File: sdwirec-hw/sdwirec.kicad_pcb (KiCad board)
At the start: 4 copper layers, 23.4 x 49.4 mm, 61 parts, among them IC1 USB2640-HZH-02, IC2 MC74HC1G04DTT1G, J1 USB_C_Receptacle_USB2.0, J2 usd_plug, J3 Micro_SD_Card, Q1 SMMBT4403L, Q2 SMMBT4403L, U1 M24C02-RDW, U2 SPX3819M5-L-3-3, U3 TS3A27518EPW, U4 FT200XD, Y1 24Mhz

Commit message: Rev 1.2
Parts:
- added C26: 4.7uF, Capacitor_SMD:C_0603_1608Metric, F.Cu at (143.8, 104.1)
- added C27: 4.7uF, Capacitor_SMD:C_0603_1608Metric, F.Cu at (156.5, 109.2)
- added C28: 100nF, Capacitor_SMD:C_0402_1005Metric, F.Cu at (154.7, 96.1)
- added C29: 100nF, Capacitor_SMD:C_0402_1005Metric, F.Cu at (146.3, 122.1)
- added G***: LOGO, sdwirec:badgerd-logo-9mm, F.Cu at (145.5, 85.2)
- added R18: 1M, Resistor_SMD:R_0402_1005Metric, F.Cu at (143.1, 110.0)
- added R19: 0R, Resistor_SMD:R_0402_1005Metric, F.Cu at (157.2, 113.2)
- added REF**: Tab, KiKit:Tab, F.Cu at (159.0, 102.9)
- added REF**: Tab, KiKit:Tab, F.Cu at (132.5, 116.3)
- added REF**: Tab, KiKit:Tab, F.Cu at (132.5, 102.9)
- added REF**: Tab, KiKit:Tab, F.Cu at (159.0, 116.3)
- added REF**: ESD-Logo_6.6x6mm_SilkScreen, Symbol:ESD-Logo_6.6x6mm_SilkScreen, B.Cu at (146.6, 94.7)
- D1: value LED_Small -> Red
- D3: value Green -> Blue
- FB1, FB2: value 180R -> 150R; footprint LED_SMD:LED_0603_1608Metric -> Diode_SMD:D_0603_1608Metric
- moved C15 6.75 mm to (156.1, 104.5), turned to 90 degrees
- moved C12 3.13 mm to (156.1, 107.0)
- moved C3 3.06 mm to (138.2, 110.5), turned to -90 degrees
- moved C19 1.60 mm to (143.7, 106.5), turned to 180 degrees
- moved R5 1.10 mm to (143.7, 107.8), turned to 0 degrees
- moved C6 0.63 mm to (140.6, 113.0)
- moved Y1 0.56 mm to (140.6, 110.3)
- moved C14 0.22 mm to (142.1, 114.7)
- moved C10 0.18 mm to (143.3, 114.7)
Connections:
- IC1 pad 13: unconnected-(IC1-Pad13) -> Net-(IC1-Pad13)
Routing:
- net +3V3: track 144.3 -> 165.0 mm, vias 19 -> 21
- net Net-(IC1-Pad13): track 0.00 -> 5.39 mm
- net /dSD_DAT3: track 20.7 -> 25.7 mm
- net GND: track 78.0 -> 82.8 mm, vias 35 -> 53
- net Net-(C12-Pad1): track 3.51 -> 8.23 mm
- net /dSD_DAT0: track 21.8 -> 25.6 mm
- net /SD_nCD: track 29.3 -> 33.1 mm
- net /dSD_DAT2: track 22.1 -> 25.7 mm
- net Net-(C29-Pad1): track 18.7 -> 20.7 mm
- net /dSD_CLK: track 23.8 -> 25.7 mm
- net /dSD_DAT1: track 24.1 -> 25.7 mm
- net /VDD: track 20.9 -> 22.2 mm
- net /USB_UP-: track 13.5 -> 12.4 mm
- net /nRESET: track 3.48 -> 2.61 mm
- net /XTAL2: track 8.52 -> 9.11 mm
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- added copper zone on B.Cu, net GND
- added copper zone on F.Cu, net GND
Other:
- board size 23.4 x 49.4 mm -> 26 x 49.9 mm
- board text added: "Rev. 1.2"
- board text added: "`"

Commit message: Rev 1.3
Signed-off-by: Talha Can Havadar <talha.can.havadar@canonical.com>
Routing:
- net GND: vias 53 -> 54
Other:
- board text added: "+"
- board text added: "Rev. 1.3"
- board text removed: "Rev. 1.2"

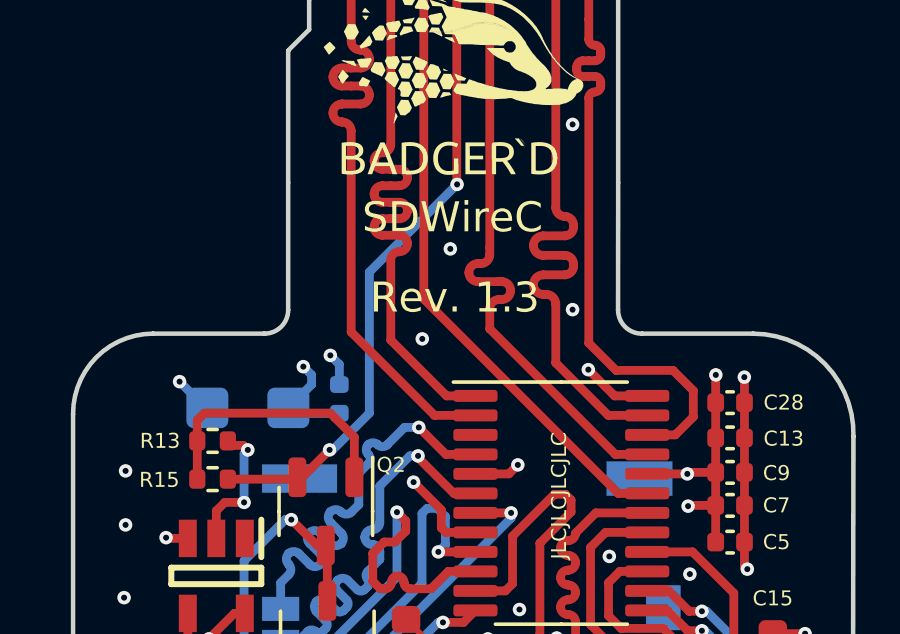
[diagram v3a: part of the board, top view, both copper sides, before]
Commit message: squash! add schottky diode on vdd_device line
Signed-off-by: Talha Can Havadar <havadartalha@gmail.com>
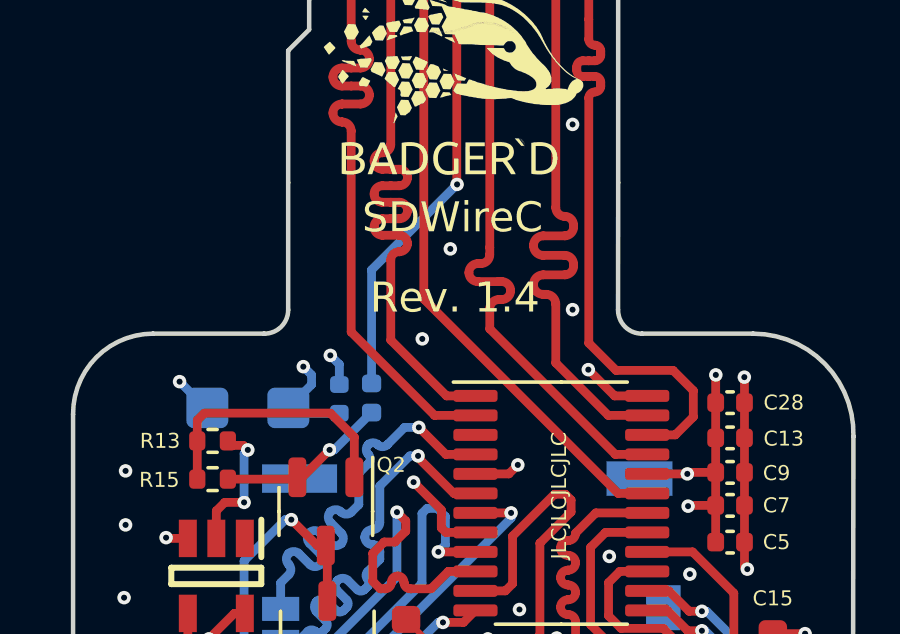
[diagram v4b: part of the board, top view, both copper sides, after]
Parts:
- added D5: D_Schottky_Small_Filled, Diode_SMD:D_0402_1005Metric, B.Cu at (142.7, 95.9)
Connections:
- J2 pad 4: /VDD_DEVICE -> Net-(J2-Pad4)
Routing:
- net /VDD_DEVICE: track 26.6 -> 5.71 mm, vias 2 -> 1
- net Net-(J2-Pad4): track 0.00 -> 19.9 mm, vias 0 -> 1
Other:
- board text added: "Rev. 1.4"
- board text removed: "Rev. 1.3"
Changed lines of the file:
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@@
   (title_block
     (title "Badgerd-SDWireC")
-    (date "2023-07-17")
-    (rev "1.3")
+    (date "2024-09-06")
+    (rev "1.4")
     (company "Badgerd Technologies B.V.")
     (comment 1 "Talha Can Havadar")
@@
   (net 77 "Net-(Q1-Pad1)")
   (net 78 "Net-(IC1-Pad13)")
+  (net 79 "Net-(J2-Pad4)")
   (footprint "KiKit:Tab" (layer "F.Cu")
     (at 159.03 102.9 180)
@@
     (property "Sheetfile" "sdwirec.kicad_sch")
     (property "Sheetname" "")
-    (attr through_hole exclude_from_pos_files)
+    (attr through_hole exclude_from_pos_files exclude_from_bom)
     (fp_text reference "J2" (at 3.79 2.35) (layer "F.SilkS") hide
       (effects (font (size 1 1) (thickness 0.15)))
@@
       (net 58 "/dSD_CMD") (pinfunction "Pin_3") (pintype "passive"))
     (pad "4" smd rect (at 3.3 -0.15) (size 0.8 3.2) (layers "F.Cu" "F.Mask")
-      (net 59 "/VDD_DEVICE") (pinfunction "Pin_4") (pintype "passive"))
+      (net 79 "Net-(J2-Pad4)") (pinfunction "Pin_4") (pintype "passive"))
     (pad "5" smd rect (at 4.4 0) (size 0.8 2.9) (layers "F.Cu" "F.Mask")
       (net 60 "/dSD_CLK") (pinfunction "Pin_5") (pintype "passive"))
@@
     )
   )
+  (footprint "Diode_SMD:D_0402_1005Metric" (layer "B.Cu")
+    (at 142.7 95.92 90)
+    (descr "Diode SMD 0402 (1005 Metric), square (rectangular) end terminal, IPC_7351 nominal, (Body size source: http://www.tortai-tech.com/upload/download/2011102023233369053.pdf), generated with kicad-footprint-generator")
+    (tags "diode")
+    (property "LCSC Part" "C2837790")
+    (property "Sheetfile" "sdwirec.kicad_sch")
+    (property "Sheetname" "")
+    (attr smd)
+    (fp_text reference "D5" (at 0 1.17 90) (layer "B.SilkS")
+      (effects (font (size 0.5 0.5) (thickness 0.1)) (justify mirror))
+    )
+    (fp_text value "D_Schottky_Small_Filled" (at 0 -1.17 90) (layer "B.Fab")
+      (effects (font (size 1 1) (thickness 0.15)) (justify mirror))
+    )
+    (fp_text user "${REFERENCE}" (at 0 0 90) (layer "B.Fab")
+      (effects (font (size 0.25 0.25) (thickness 0.04)) (justify mirror))
+    )
+    (fp_circle (center -1.09 0) (end -1.04 0) (layer "B.SilkS") (width 0.1) (fill none))
+    (fp_line (start -0.93 -0.47) (end -0.93 0.47) (layer "B.CrtYd") (width 0.05))
+    (fp_line (start -0.93 0.47) (end 0.93 0.47) (layer "B.CrtYd") (width 0.05))
+    (fp_line (start 0.93 -0.47) (end -0.93 -0.47) (layer "B.CrtYd") (width 0.05))
+    (fp_line (start 0.93 0.47) (end 0.93 -0.47) (layer "B.CrtYd") (width 0.05))
+    (fp_line (start 0.5 -0.25) (end -0.5 -0.25) (layer "B.Fab") (width 0.1))
+    (fp_line (start -0.4 -0.25) (end -0.4 0.25) (layer "B.Fab") (width 0.1))
+    (fp_line (start 0.5 0.25) (end 0.5 -0.25) (layer "B.Fab") (width 0.1))
+    (fp_line (start -0.5 -0.25) (end -0.5 0.25) (layer "B.Fab") (width 0.1))
+    (fp_line (start -0.5 0.25) (end 0.5 0.25) (layer "B.Fab") (width 0.1))
+    (fp_line (start -0.3 -0.25) (end -0.3 0.25) (layer "B.Fab") (width 0.1))
+    (pad "1" smd roundrect (at -0.485 0 90) (size 0.59 0.64) (layers "B.Cu" "B.Paste" "B.Mask") (roundrect_rratio 0.25)
+      (net 59 "/VDD_DEVICE") (pinfunction "K") (pintype "passive"))
+    (pad "2" smd roundrect (at 0.485 0 90) (size 0.59 0.64) (layers "B.Cu" "B.Paste" "B.Mask") (roundrect_rratio 0.25)
+      (net 79 "Net-(J2-Pad4)") (pinfunction "A") (pintype "passive"))
+    (model "${KICAD6_3DMODEL_DIR}/Diode_SMD.3dshapes/D_0402_1005Metric.wrl"
+      (offset (xyz 0 0 0))
+      (scale (xyz 1 1 1))
+      (rotate (xyz 0 0 0))
+    )
+  )
   (footprint "sdwirec:5031821852" (layer "B.Cu")
     (at 140.3 105.8 -90)
@@
     (effects (font (size 1 1) (thickness 0.15)))
   )
-  (gr_text "Rev. 1.3" (at 145.475 92.575) (layer "F.SilkS")
+  (gr_text "Rev. 1.4" (at 145.475 92.575) (layer "F.SilkS")
     (effects (font (size 1 1) (thickness 0.15)))
   )
@@
   (segment (start 150.92 99.1) (end 151.8875 99.1) (width 0.29337) (layer "F.Cu") (net 58))
   (segment (start 144.44 92.62) (end 150.92 99.1) (width 0.29337) (layer "F.Cu") (net 58))
-  (segment (start 145.54 88.79) (end 145.54 76.685) (width 0.29337) (layer "F.Cu") (net 59))
   (segment (start 137.91 98.625) (end 140.1625 98.625) (width 0.29337) (layer "F.Cu") (net 59))
-  (segment (start 145.55 88.8) (end 145.54 88.79) (width 0.29337) (layer "F.Cu") (net 59))
   (segment (start 140.1625 98.625) (end 140.225 98.5625) (width 0.29337) (layer "F.Cu") (net 59))
   (segment (start 140.3875 98.5625) (end 141.3 97.65) (width 0.29337) (layer "F.Cu") (net 59))
   (segment (start 140.225 98.5625) (end 140.3875 98.5625) (width 0.29337) (layer "F.Cu") (net 59))
-  (via (at 145.55 88.8) (size 0.45) (drill 0.2) (layers "F.Cu" "B.Cu") (net 59))
   (via (at 141.3 97.65) (size 0.45) (drill 0.2) (layers "F.Cu" "B.Cu") (net 59))
-  (segment (start 142.625 91.725) (end 142.625 96.428277) (width 0.29337) (layer "B.Cu") (net 59))
-  (segment (start 141.403277 97.65) (end 141.3 97.65) (width 0.29337) (layer "B.Cu") (net 59))
-  (segment (start 145.55 88.8) (end 142.625 91.725) (width 0.29337) (layer "B.Cu") (net 59))
-  (segment (start 142.625 96.428277) (end 141.403277 97.65) (width 0.29337) (layer "B.Cu") (net 59))
+  (segment (start 141.3 97.65) (end 141.455 97.65) (width 0.29337) (layer "B.Cu") (net 59))
+  (segment (start 141.455 97.65) (end 142.7 96.405) (width 0.29337) (layer "B.Cu") (net 59))
   (segment (start 147.035398 92.04) (end 146.94 92.04) (width 0.29337) (layer "F.Cu") (net 60))
   (segment (start 146.244602 91.44) (end 146.34 91.44) (width 0.29337) (layer "F.Cu") (net 60))
@@
   (segment (start 156.225 111.575) (end 153.675 111.575) (width 0.29337) (layer "F.Cu") (net 78))
   (segment (start 157.225 112.575) (end 156.225 111.575) (width 0.29337) (layer "F.Cu") (net 78))
+  (segment (start 145.54 88.79) (end 145.54 76.685) (width 0.29337) (layer "F.Cu") (net 79))
+  (segment (start 145.55 88.8) (end 145.54 88.79) (width 0.29337) (layer "F.Cu") (net 79))
+  (via (at 145.55 88.8) (size 0.45) (drill 0.2) (layers "F.Cu" "B.Cu") (net 79))
+  (segment (start 142.7 95.435) (end 142.7 91.65) (width 0.29337) (layer "B.Cu") (net 79))
+  (segment (start 142.7 91.65) (end 145.55 88.8) (width 0.29337) (layer "B.Cu") (net 79))
   (zone (net 0) (net_name "") (layers "F.Cu" "In1.Cu" "In2.Cu" "B.Cu") (hatch edge 0.508)
     (connect_pads (clearance 0))
